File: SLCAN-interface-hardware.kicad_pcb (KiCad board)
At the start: 2 copper layers, 42 x 37 mm, 25 parts, among them J1 DE9_Plug_MountingHoles, J2 Conn_01x06, SW1 MSS22D18, U1 ProMicro, U2 MCP2515-xSO, U3 TJA1051T, Y1 8Mhz

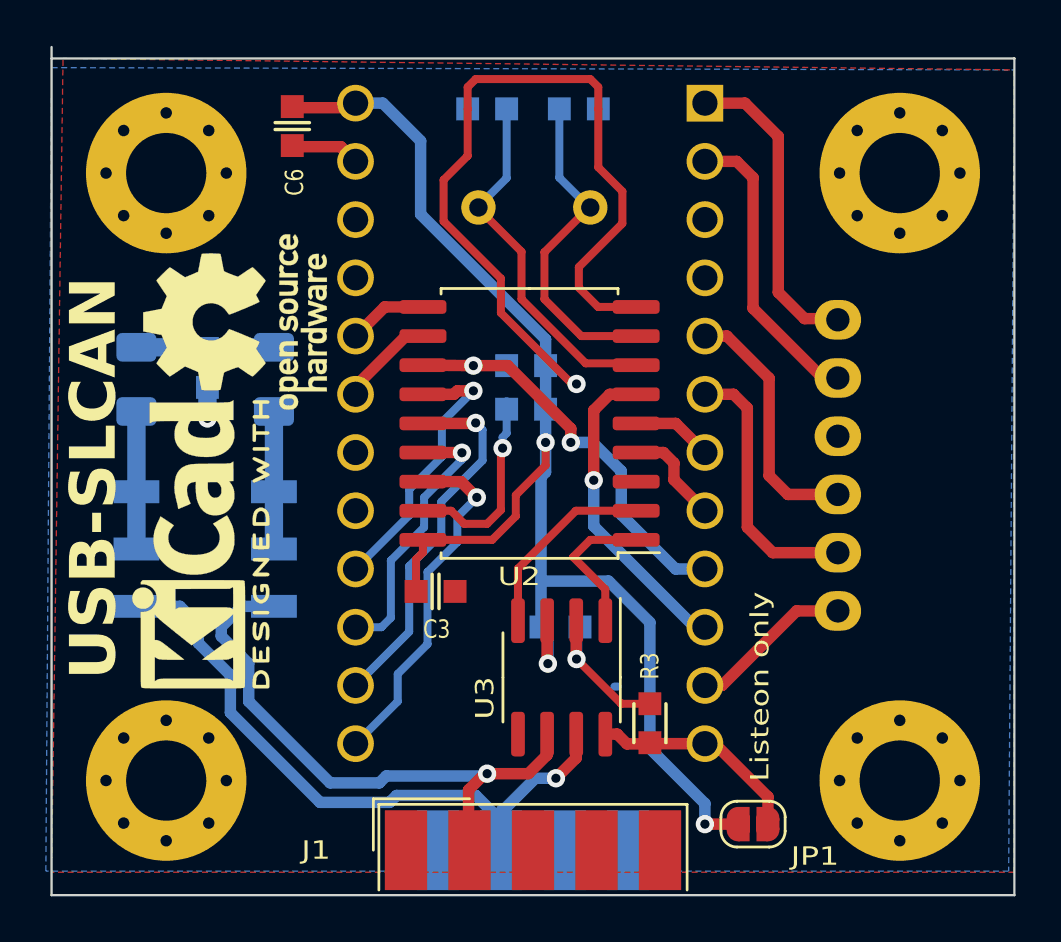
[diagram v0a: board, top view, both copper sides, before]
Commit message: Add step model
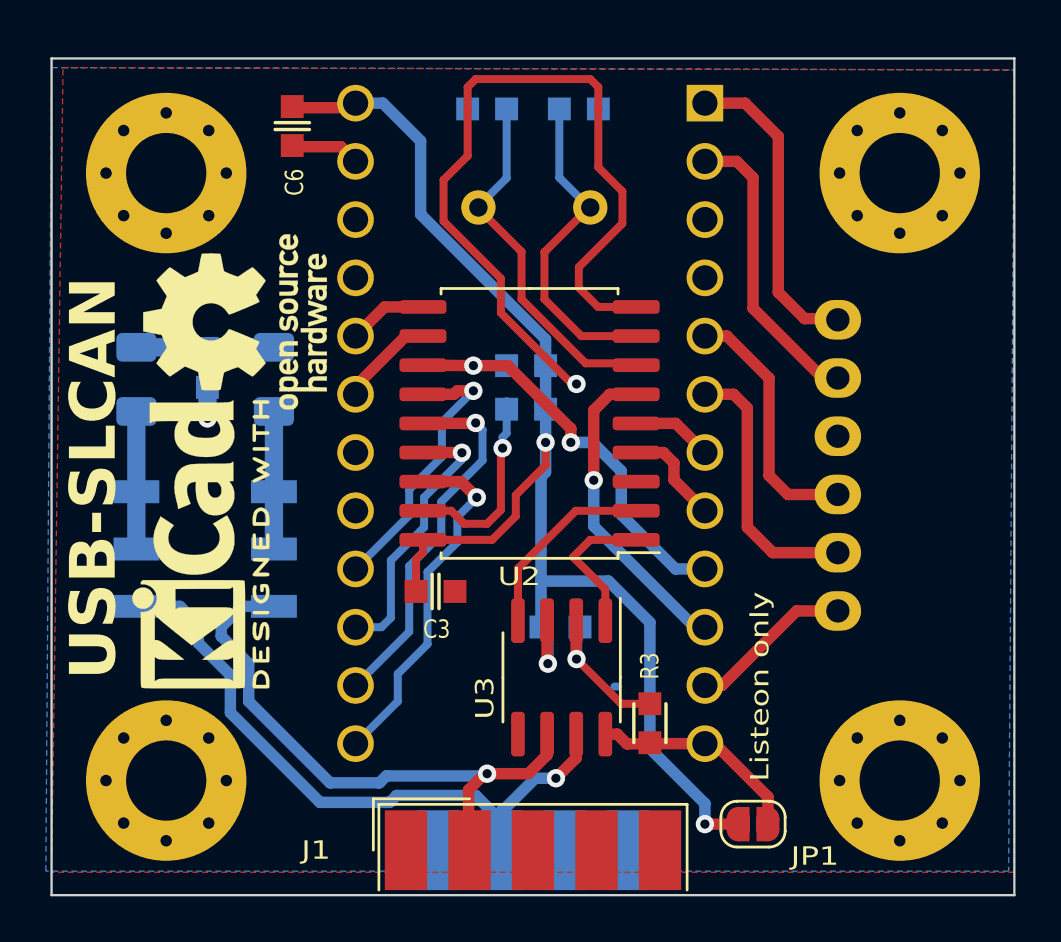
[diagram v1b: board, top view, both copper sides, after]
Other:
- board size 42 x 37 mm -> 42 x 36.5 mm
